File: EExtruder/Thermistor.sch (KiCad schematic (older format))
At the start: 5 parts, among them J5 Conn_01x02

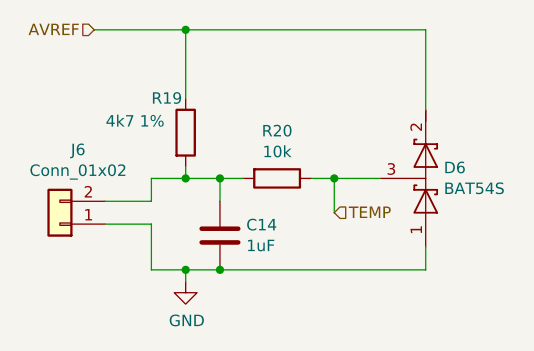
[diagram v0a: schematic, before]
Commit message: Select correct terminals. Use old style square footprints.
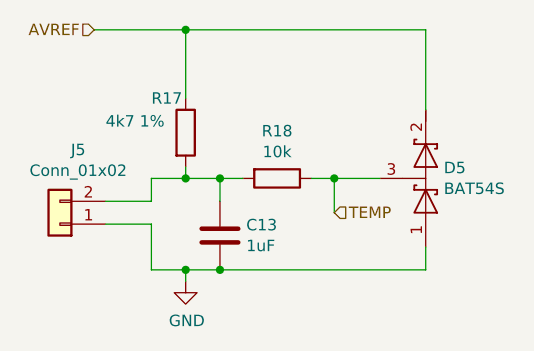
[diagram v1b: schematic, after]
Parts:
- C13: footprint Capacitor_SMD:C_0603_1608Metric -> Local:C_0603_1608Metric
- R17, R18: footprint Resistor_SMD:R_0603_1608Metric -> Local:R_0603_1608Metric
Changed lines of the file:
@@
 $Descr A4 11693 8268
 encoding utf-8
-Sheet 5 8
+Sheet 4 8
 Title ""
 Date ""
@@
 AR Path="/5BBB446C/5BBB4586" Ref="R17"  Part="1"
 AR Path="/5BBB560B/5BBB4586" Ref="R19"  Part="1"
-F 0 "R19" H 5100 2400 50  0000 L CNN
+F 0 "R17" H 5100 2400 50  0000 L CNN
 F 1 "4k7 1%" H 4900 2300 50  0000 L CNN
-F 2 "Resistor_SMD:R_0603_1608Metric" V 5180 2250 50  0001 C CNN
+F 2 "Local:R_0603_1608Metric" V 5180 2250 50  0001 C CNN
 F 3 "~" H 5250 2250 50  0001 C CNN
 	1    5250 2250
@@
 AR Path="/5BBB446C/5BBB460D" Ref="R18"  Part="1"
 AR Path="/5BBB560B/5BBB460D" Ref="R20"  Part="1"
-F 0 "R20" V 5443 2450 50  0000 C CNN
+F 0 "R18" V 5443 2450 50  0000 C CNN
 F 1 "10k" V 5534 2450 50  0000 C CNN
-F 2 "Resistor_SMD:R_0603_1608Metric" V 5580 2450 50  0001 C CNN
+F 2 "Local:R_0603_1608Metric" V 5580 2450 50  0001 C CNN
 F 3 "~" H 5650 2450 50  0001 C CNN
 	1    5650 2450
@@
 AR Path="/5BBB446C/5BBB4655" Ref="C13"  Part="1"
 AR Path="/5BBB560B/5BBB4655" Ref="C14"  Part="1"
-F 0 "C14" H 5515 2746 50  0000 L CNN
+F 0 "C13" H 5515 2746 50  0000 L CNN
 F 1 "1uF" H 5515 2655 50  0000 L CNN
-F 2 "Capacitor_SMD:C_0603_1608Metric" H 5438 2550 50  0001 C CNN
+F 2 "Local:C_0603_1608Metric" H 5438 2550 50  0001 C CNN
 F 3 "~" H 5400 2700 50  0001 C CNN
 	1    5400 2700
@@
 AR Path="/5BBB446C/5BBB47CD" Ref="J5"  Part="1"
 AR Path="/5BBB560B/5BBB47CD" Ref="J6"  Part="1"
-F 0 "J6" H 4620 2325 50  0000 C CNN
+F 0 "J5" H 4620 2325 50  0000 C CNN
 F 1 "Conn_01x02" H 4620 2416 50  0000 C CNN
 F 2 "Connector_PinHeader_2.54mm:PinHeader_1x02_P2.54mm_Vertical" H 4700 2650 50  0001 C CNN
@@
 AR Path="/5BBB446C/5BBB4CDD" Ref="D5"  Part="1"
 AR Path="/5BBB560B/5BBB4CDD" Ref="D6"  Part="1"
-F 0 "D6" V 6346 2529 50  0000 L CNN
+F 0 "D5" V 6346 2529 50  0000 L CNN
 F 1 "BAT54S" V 6255 2529 50  0000 L CNN
 F 2 "Package_TO_SOT_SMD:SOT-23" H 6300 2450 50  0001 C CNN

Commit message: Add solder jumper on the audio jack to avoid ground loops.
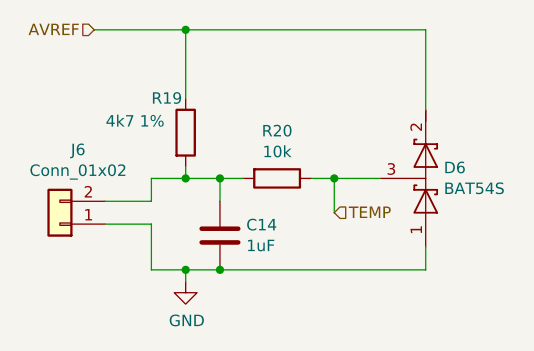
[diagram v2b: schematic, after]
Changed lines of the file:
@@
 AR Path="/5BBB446C/5BBB4586" Ref="R17"  Part="1"
 AR Path="/5BBB560B/5BBB4586" Ref="R19"  Part="1"
-F 0 "R17" H 5100 2400 50  0000 L CNN
+F 0 "R19" H 5100 2400 50  0000 L CNN
 F 1 "4k7 1%" H 4900 2300 50  0000 L CNN
 F 2 "Local:R_0603_1608Metric" V 5180 2250 50  0001 C CNN
@@
 AR Path="/5BBB446C/5BBB460D" Ref="R18"  Part="1"
 AR Path="/5BBB560B/5BBB460D" Ref="R20"  Part="1"
-F 0 "R18" V 5443 2450 50  0000 C CNN
+F 0 "R20" V 5443 2450 50  0000 C CNN
 F 1 "10k" V 5534 2450 50  0000 C CNN
 F 2 "Local:R_0603_1608Metric" V 5580 2450 50  0001 C CNN
@@
 AR Path="/5BBB446C/5BBB4655" Ref="C13"  Part="1"
 AR Path="/5BBB560B/5BBB4655" Ref="C14"  Part="1"
-F 0 "C13" H 5515 2746 50  0000 L CNN
+F 0 "C14" H 5515 2746 50  0000 L CNN
 F 1 "1uF" H 5515 2655 50  0000 L CNN
 F 2 "Local:C_0603_1608Metric" H 5438 2550 50  0001 C CNN
@@
 AR Path="/5BBB446C/5BBB47CD" Ref="J5"  Part="1"
 AR Path="/5BBB560B/5BBB47CD" Ref="J6"  Part="1"
-F 0 "J5" H 4620 2325 50  0000 C CNN
+F 0 "J6" H 4620 2325 50  0000 C CNN
 F 1 "Conn_01x02" H 4620 2416 50  0000 C CNN
 F 2 "Connector_PinHeader_2.54mm:PinHeader_1x02_P2.54mm_Vertical" H 4700 2650 50  0001 C CNN
@@
 AR Path="/5BBB446C/5BBB4CDD" Ref="D5"  Part="1"
 AR Path="/5BBB560B/5BBB4CDD" Ref="D6"  Part="1"
-F 0 "D5" V 6346 2529 50  0000 L CNN
+F 0 "D6" V 6346 2529 50  0000 L CNN
 F 1 "BAT54S" V 6255 2529 50  0000 L CNN
 F 2 "Package_TO_SOT_SMD:SOT-23" H 6300 2450 50  0001 C CNN
